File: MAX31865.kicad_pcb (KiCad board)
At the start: 2 copper layers, 25.4 x 27.9 mm, 29 parts, among them U1 MAX31865, U3 MIC5225-3.3, X1 3.5mm, X2 3.5mm

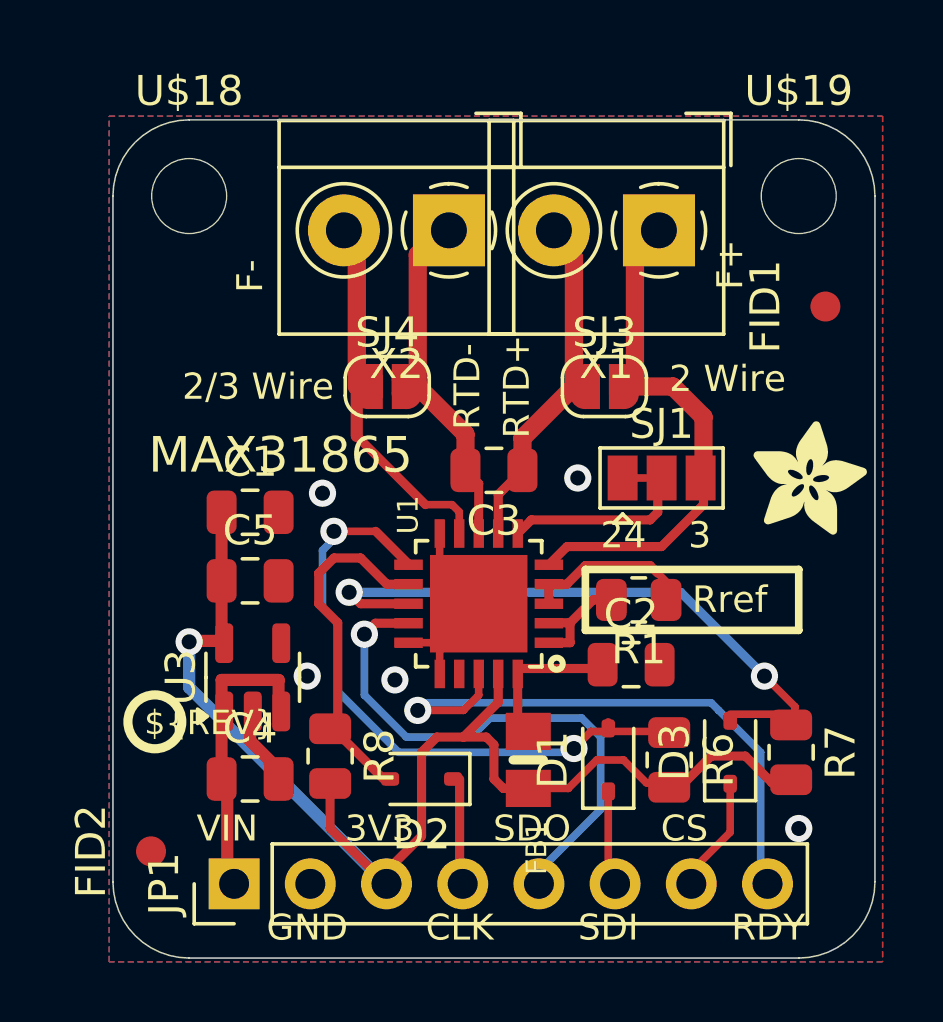
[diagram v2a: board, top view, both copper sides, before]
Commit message: fixed routing + added BOM info
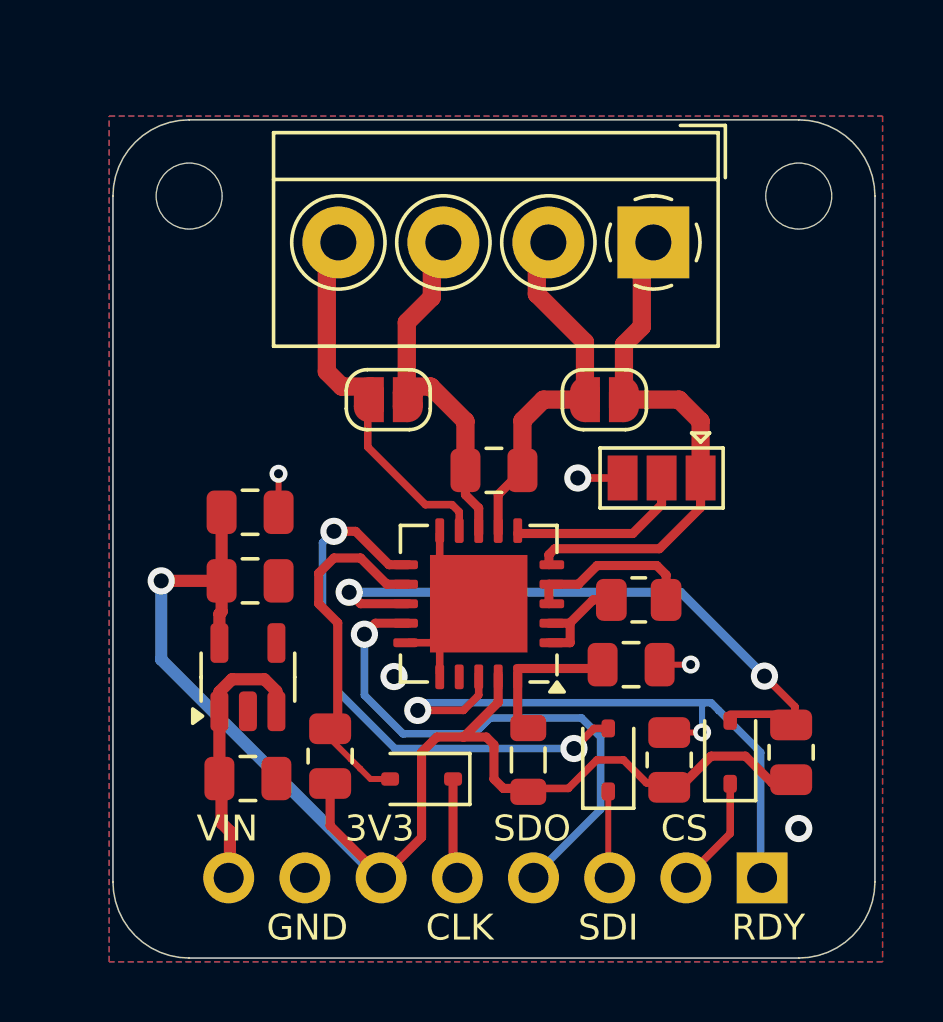
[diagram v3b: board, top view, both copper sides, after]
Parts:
- removed FID1, FID2: FIDUCIAL"", Fiducial:Fiducial_1mm_Mask2mm
- removed U$16: , ADAFRUIT_3.5MM
- removed U$20, U$21: , ADAFRUIT_5MM
- removed U$8: , PCBFEAT-REV-040
- removed X1, X2: 3.5mm, TerminalBlock_4Ucon:TerminalBlock_4Ucon_1x02_P3.50mm_Horizontal
- added J2: Screw_Terminal_01x04, TerminalBlock_4Ucon:TerminalBlock_4Ucon_1x04_P3.50mm_Horizontal, F.Cu at (153.8, 95.1)
- FB1: value (none) -> FERRITE-0805NO; footprint 0805-NO -> Inductor_SMD:L_0805_2012Metric
- J1: renamed from JP1; value (none) -> <; moved to B.Cu
- SJ1: value (none) -> SOLDERJUMPER_2WAY
- SJ3, SJ4: value (none) -> SOLDERJUMPER
- U$18, U$19: footprint MountingHole:MountingHole_2.5mm -> MountingHole:MountingHole_2.2mm_M2_ISO7380
- U1: value MAX31865 -> l; footprint QFN20_4MM_0.65MM -> Package_DFN_QFN:TQFN-20-1EP_5x5mm_P0.65mm_EP3.25x3.25mm
- moved J1 17.6 mm to (157.4, 116.3)
- moved SJ4 0.44 mm to (145.0, 100.4)
- moved SJ3 0.44 mm to (152.2, 100.4)
- moved U2 0.16 mm to (140.3, 109.6)
- moved C4 0.07 mm to (140.3, 113.0)
- turned SJ1 to 180 degrees
- turned U1 to 180 degrees
- renumbered U3 to U2
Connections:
- net FORCE- renamed Net-(J2-Pin_4)
- net RTDIN+ renamed Net-(J2-Pin_2)
- net RTDIN- renamed Net-(J2-Pin_3)
- D1 pad 1: (no net) -> /SDI_5V
- D1 pad 2: (no net) -> Net-(D1-A)
- D2 pad 1: (no net) -> /SCLK_5V
- D2 pad 2: (no net) -> Net-(D2-A)
- D3 pad 1: (no net) -> /CS_5V
- D3 pad 2: (no net) -> Net-(D3-A)
- J1 pad 1: VIN -> /DRDY
- J1 pad 2: GND -> /CS_5V
- J1 pad 3: VDD -> /SDI_5V
- J1 pad 4: SCLK_5V -> /SDO
- J1 pad 5: SDO -> /SCLK_5V
- J1 pad 6: SDI_5V -> VDD
- J1 pad 7: CS_5V -> GND
- J1 pad 8: DRDY -> VIN
- R6 pad 1: N$14 -> /DRDY
- R7 pad 1: N$12 -> Net-(D3-A)
- R8 pad 1: N$13 -> Net-(D2-A)
- SJ1 pad 1: GND -> Net-(J2-Pin_1)
- SJ1 pad 3: FORCE+ -> GND
- SJ3 pad 2: FORCE+ -> Net-(J2-Pin_1)
- U1 pad 11: N$14 -> Net-(D1-A)
- U1 pad 12: N$13 -> Net-(D2-A)
- U1 pad 13: N$12 -> Net-(D3-A)
- U1 pad 14: SDO -> /SDO
- U1 pad 17: (no net) -> unconnected-(U1-NC-Pad17)
- U1 pad 18: DRDY -> /DRDY
- U1 pad 5: FORCE+ -> Net-(J2-Pin_1)
- U2 pad 4: (no net) -> unconnected-(U2-P4-Pad4)
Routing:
- net N$14: track 21.5 -> 0.00 mm, vias 2 -> 0
- net /DRDY: track 0.00 -> 21.4 mm, vias 0 -> 2
- net Net-(D3-A): track 0.00 -> 21.4 mm, vias 0 -> 2
- net N$12: track 21.4 -> 0.00 mm, vias 2 -> 0
- net DRDY: track 19.4 -> 0.00 mm, vias 1 -> 0
- net SDO: track 18.8 -> 0.00 mm, vias 1 -> 0
- net Net-(D1-A): track 0.00 -> 18.7 mm, vias 0 -> 2
- net /SDO: track 0.00 -> 18.7 mm, vias 0 -> 1
- net FORCE+: track 17.0 -> 0.00 mm
- net Net-(J2-Pin_1): track 0.00 -> 16.6 mm
- net Net-(D2-A): track 0.00 -> 12.0 mm
- net N$13: track 11.6 -> 0.00 mm
- net CS_5V: track 3.55 -> 0.00 mm
- net /CS_5V: track 0.00 -> 3.53 mm
- net SCLK_5V: track 3.43 -> 0.00 mm
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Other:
- board text removed: "2 Wire"
- board text removed: "2/3 Wire"
- board text removed: "2/3/4 Wire Platinum RTD Converter"
- board text removed: "24"
- board text removed: "3"
- board text removed: "F+"
- board text removed: "F-"
- board text removed: "MAX31865"
- board text removed: "RTD+"
- board text removed: "RTD-"
- board text removed: "Rref"
- board text removed: "Vin: 3-5VDC Vlogic: 3-5VDC"

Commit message: removed imported library
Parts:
- C3: value 100nF -> 0.1uF
- J1: value < -> connector
- R1: value 430Ω / 4300Ω 0.1% -> 430Ω, ±0.1%
- U1: value l -> MAX31865
- U2: value MIC5225-3.3 -> MIC5225
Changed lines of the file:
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@@
 			)
 		)
-		(property "Description" "Resistor"
+		(property "Description" "SMD Chip Resistor, 10 kohm, ± 1%, 125 mW, 0805 [2012 Metric], Thick Film, General Purpose"
 			(at 0 0 -90)
 			(unlocked yes)
@@
 			)
 		)
-		(property "MPN" ""
+		(property "MPN" "/"
 			(at 0 0 -90)
 			(unlocked yes)
@@
 			)
 		)
-		(property "Manufacturer" ""
+		(property "Manufacturer" "/"
 			(at 0 0 -90)
 			(unlocked yes)
@@
 			)
 		)
-		(property "SPN" ""
+		(property "SPN" "GPR080510K"
 			(at 0 0 -90)
 			(unlocked yes)
@@
 			)
 		)
-		(property "Supplier" ""
+		(property "Supplier" "Eurocircuits"
 			(at 0 0 -90)
 			(unlocked yes)
@@
 		(sheetfile "MAX31865.kicad_sch")
 		(zone_connect 1)
-		(attr exclude_from_pos_files)
+		(attr exclude_from_pos_files exclude_from_bom)
 		(fp_line
 			(start 2.05 1)
@@
 			)
 		)
-		(property "Description" "Resistor"
+		(property "Description" "SMD Chip Resistor, 10 kohm, ± 1%, 125 mW, 0805 [2012 Metric], Thick Film, General Purpose"
 			(at 0 0 -90)
 			(unlocked yes)
@@
 			)
 		)
-		(property "MPN" ""
+		(property "MPN" "/"
 			(at 0 0 -90)
 			(unlocked yes)
@@
 			)
 		)
-		(property "Manufacturer" ""
+		(property "Manufacturer" "/"
 			(at 0 0 -90)
 			(unlocked yes)
@@
 			)
 		)
-		(property "SPN" ""
+		(property "SPN" "GPR080510K"
 			(at 0 0 -90)
 			(unlocked yes)
@@
 			)
 		)
-		(property "Supplier" ""
+		(property "Supplier" "Eurocircuits"
 			(at 0 0 -90)
 			(unlocked yes)
@@
 		(sheetfile "MAX31865.kicad_sch")
 		(zone_connect 1)
-		(attr exclude_from_pos_files)
+		(attr exclude_from_pos_files exclude_from_bom)
 		(fp_line
 			(start -1.4 0.3)
@@
 			)
 		)
-		(property "Value" "430Ω / 4300Ω 0.1%"
+		(property "Value" "430Ω, ±0.1%"
 			(at 0 1.65 180)
 			(layer "F.Fab")
@@
 			)
 		)
-		(property "Description" "Resistor, small symbol"
+		(property "Description" "SMD Chip Resistor, 430 ohm, ± 1%, 125 mW, 0805 [2012 Metric], Thick Film, General Purpose"
 			(at 0 0 180)
 			(unlocked yes)
@@
 			)
 		)
-		(property "MPN" ""
+		(property "MPN" "/"
 			(at 0 0 180)
 			(unlocked yes)
@@
 			)
 		)
-		(property "Manufacturer" ""
+		(property "Manufacturer" "/"
 			(at 0 0 180)
 			(unlocked yes)
@@
 			)
 		)
-		(property "SPN" ""
+		(property "SPN" "GPR0805430R"
 			(at 0 0 180)
 			(unlocked yes)
@@
 			)
 		)
-		(property "Supplier" ""
+		(property "Supplier" "Eurocircuits"
 			(at 0 0 180)
 			(unlocked yes)
@@
 			)
 		)
-		(property "Value" "l"
+		(property "Value" "MAX31865"
 			(at 0 3.8 180)
 			(layer "F.Fab")
@@
 			)
 		)
-		(property "Description" "RTD-to-Digital Converter, TQFN-20"
+		(property "Description" "IC RTD TO DIGITAL CONVERT 20QFN"
 			(at 0 0 180)
 			(unlocked yes)
@@
 			)
 		)
-		(property "Component package type" ""
+		(property "Component package type" "20-TQFN (5x5)"
 			(at 0 0 180)
 			(unlocked yes)
@@
 			)
 		)
-		(property "MPN" ""
+		(property "MPN" "MAX31865ATP+"
 			(at 0 0 180)
 			(unlocked yes)
@@
 			)
 		)
-		(property "Manufacturer" ""
+		(property "Manufacturer" "Analog Devices Inc./Maxim Integrated"
 			(at 0 0 180)
 			(unlocked yes)
@@
 			)
 		)
-		(property "SPN" ""
+		(property "SPN" "MAX31865ATP+-ND"
 			(at 0 0 180)
 			(unlocked yes)
@@
 			)
 		)
-		(property "Supplier" ""
+		(property "Supplier" "DigiKey"
 			(at 0 0 180)
 			(unlocked yes)
@@
 			)
 		)
-		(property "Value" "MIC5225-3.3"
+		(property "Value" "MIC5225"
 			(at 0 2.4 -90)
 			(layer "F.Fab")
@@
 			)
 		)
-		(property "Description" "Unpolarized capacitor, small symbol"
+		(property "Description" "0.1µF ±10% 50V Ceramic Capacitor X7R 0805 (2012 Metric)"
 			(at 0 0 0)
 			(unlocked yes)
@@
 			)
 		)
-		(property "MPN" ""
+		(property "MPN" "/"
 			(at 0 0 0)
 			(unlocked yes)
@@
 			)
 		)
-		(property "Manufacturer" ""
+		(property "Manufacturer" "/"
 			(at 0 0 0)
 			(unlocked yes)
@@
 			)
 		)
-		(property "SPN" ""
+		(property "SPN" "GPC0805104"
 			(at 0 0 0)
 			(unlocked yes)
@@
 			)
 		)
-		(property "Supplier" ""
+		(property "Supplier" "Eurocircuits"
 			(at 0 0 0)
 			(unlocked yes)
@@
 		(sheetfile "MAX31865.kicad_sch")
 		(zone_connect 1)
-		(attr exclude_from_pos_files)
+		(attr exclude_from_pos_files exclude_from_bom)
 		(fp_line
 			(start -1.4 0.3)
@@
 			)
 		)
-		(property "Value" "100nF"
+		(property "Value" "0.1uF"
 			(at 0 1.68 180)
 			(layer "F.Fab")
@@
 			)
 		)
-		(property "Description" "Unpolarized capacitor, small symbol"
+		(property "Description" "0.1µF ±10% 50V Ceramic Capacitor X7R 0805 (2012 Metric)"
 			(at 0 0 180)
 			(unlocked yes)
@@
 			)
 		)
-		(property "MPN" ""
+		(property "MPN" "/"
 			(at 0 0 180)
 			(unlocked yes)
@@
 			)
 		)
-		(property "Manufacturer" ""
+		(property "Manufacturer" "/"
 			(at 0 0 180)
 			(unlocked yes)
@@
 			)
 		)
-		(property "SPN" ""
+		(property "SPN" "GPC0805104"
 			(at 0 0 180)
 			(unlocked yes)
@@
 			)
 		)
-		(property "Supplier" ""
+		(property "Supplier" "Eurocircuits"
 			(at 0 0 180)
 			(unlocked yes)
@@
 			)
 		)
+		(property ki_fp_filters "MountingHole*")
+		(sheetname "Root")
+		(sheetfile "MAX31865.kicad_sch")
 		(attr exclude_from_pos_files exclude_from_bom)
 		(fp_circle
@@
 			)
 		)
-		(property "Description" "Ferrite bead, small symbol"
+		(property "Description" "FERRITE BEAD 200 OHM 0805 1LN"
 			(at 0 0 -90)
 			(unlocked yes)
@@
 			)
 		)
-		(property "MPN" ""
+		(property "MPN" "LI0805G201R-10"
 			(at 0 0 -90)
 			(unlocked yes)
@@
 			)
 		)
-		(property "Manufacturer" ""
+		(property "Manufacturer" "Laird-Signal Integrity Products"
 			(at 0 0 -90)
 			(unlocked yes)
@@
 			)
 		)
-		(property "SPN" ""
+		(property "SPN" "240-2549-2-ND"
 			(at 0 0 -90)
 			(unlocked yes)
@@
 			)
 		)
-		(property "Supplier" ""
+		(property "Supplier" "DigiKey"
 			(at 0 0 -90)
 			(unlocked yes)
@@
 			)
 		)
-		(property "Description" "Generic screw terminal, single row, 01x04, script generated (kicad-library-utils/schlib/autogen/connector/)"
+		(property "Description" "TERM BLK 4POS SIDE ENT 3.5MM PCB"
 			(at 0 0 180)
 			(unlocked yes)
@@
 			)
 		)
+		(property "MPN" "0393570004"
+			(at 0 0 180)
+			(unlocked yes)
+			(layer "F.Fab")
+			(hide yes)
+			(effects
+				(font
+					(size 1 1)
+					(thickness 0.15)
+				)
+			)
+		)
+		(property "Manufacturer" "Molex"
+			(at 0 0 180)
+			(unlocked yes)
+			(layer "F.Fab")
+			(hide yes)
+			(effects
+				(font
+					(size 1 1)
+					(thickness 0.15)
+				)
+			)
+		)
+		(property "SPN" "WM7860-ND"
+			(at 0 0 180)
+			(unlocked yes)
+			(layer "F.Fab")
+			(hide yes)
+			(effects
+				(font
+					(size 1 1)
+					(thickness 0.15)
+				)
+			)
+		)
+		(property "Supplier" "DigiKey"
+			(at 0 0 180)
+			(unlocked yes)
+			(layer "F.Fab")
+			(hide yes)
+			(effects
+				(font
+					(size 1 1)
+					(thickness 0.15)
+				)
+			)
+		)
 		(property ki_fp_filters "TerminalBlock*:*")
 		(sheetname "Root")
@@
 			)
 		)
+		(property ki_fp_filters "MountingHole*")
+		(sheetname "Root")
+		(sheetfile "MAX31865.kicad_sch")
 		(attr exclude_from_pos_files exclude_from_bom)
 		(fp_circle
@@
 			)
 		)
-		(property "Description" "Resistor"
+		(property "Description" "SMD Chip Resistor, 10 kohm, ± 1%, 125 mW, 0805 [2012 Metric], Thick Film, General Purpose"
 			(at 0 0 -90)
 			(unlocked yes)
@@
 			)
 		)
-		(property "MPN" ""
+		(property "MPN" "/"
 			(at 0 0 -90)
 			(unlocked yes)
@@
 			)
 		)
-		(property "Manufacturer" ""
+		(property "Manufacturer" "/"
 			(at 0 0 -90)
 			(unlocked yes)
@@
 			)
 		)
-		(property "SPN" ""
+		(property "SPN" "GPR080510K"
 			(at 0 0 -90)
 			(unlocked yes)
@@
 			)
 		)
-		(property "Supplier" ""
+		(property "Supplier" "Eurocircuits"
 			(at 0 0 -90)
 			(unlocked yes)
@@
 			)
 		)
-		(property "Description" "Unpolarized capacitor, small symbol"
+		(property "Description" "0.1µF ±10% 50V Ceramic Capacitor X7R 0805 (2012 Metric)"
 			(at 0 0 0)
 			(unlocked yes)
@@
 			)
 		)
-		(property "MPN" ""
+		(property "MPN" "/"
 			(at 0 0 0)
 			(unlocked yes)
@@
 			)
 		)
-		(property "Manufacturer" ""
+		(property "Manufacturer" "/"
 			(at 0 0 0)
 			(unlocked yes)
@@
 			)
 		)
-		(property "SPN" ""
+		(property "SPN" "GPC0805104"
 			(at 0 0 0)
 			(unlocked yes)
@@
 			)
 		)
-		(property "Supplier" ""
+		(property "Supplier" "Eurocircuits"
 			(at 0 0 0)
 			(unlocked yes)
@@
 			)
 		)
-		(property "Value" "<"
+		(property "Value" "connector"
 			(at 0 -20.11 -90)
 			(layer "B.Fab")
@@
 		(min_thickness 0.127)
 		(filled_areas_thickness no)
-		(fill yes
+		(fill
 			(thermal_gap 0.304)
 			(thermal_bridge_width 0.304)
@@
 		(min_thickness 0.127)
 		(filled_areas_thickness no)
-		(fill yes
+		(fill
 			(thermal_gap 0.304)
 			(thermal_bridge_width 0.304)
